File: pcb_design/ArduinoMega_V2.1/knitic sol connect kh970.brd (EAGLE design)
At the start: 40.9 x 35.5 mm, 18 parts

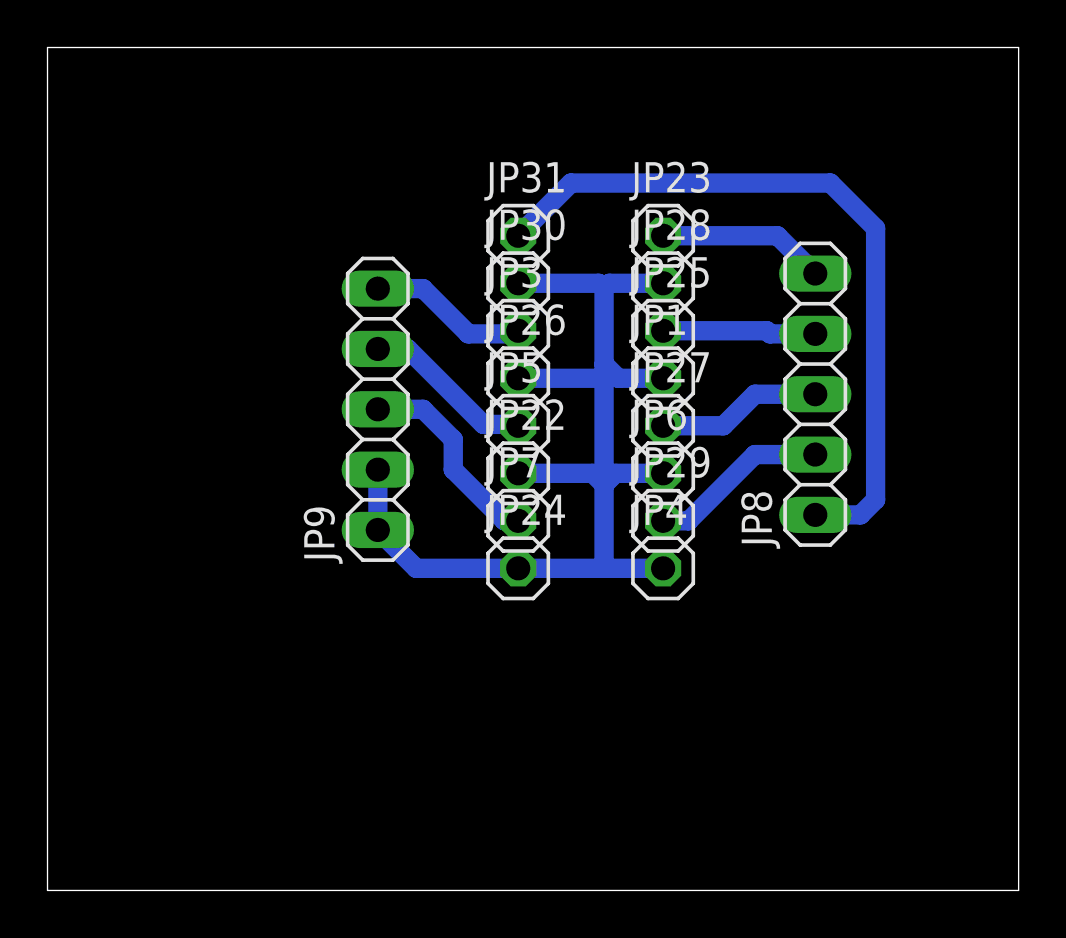
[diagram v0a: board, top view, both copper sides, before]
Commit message: Add info and reset/led on pcb design
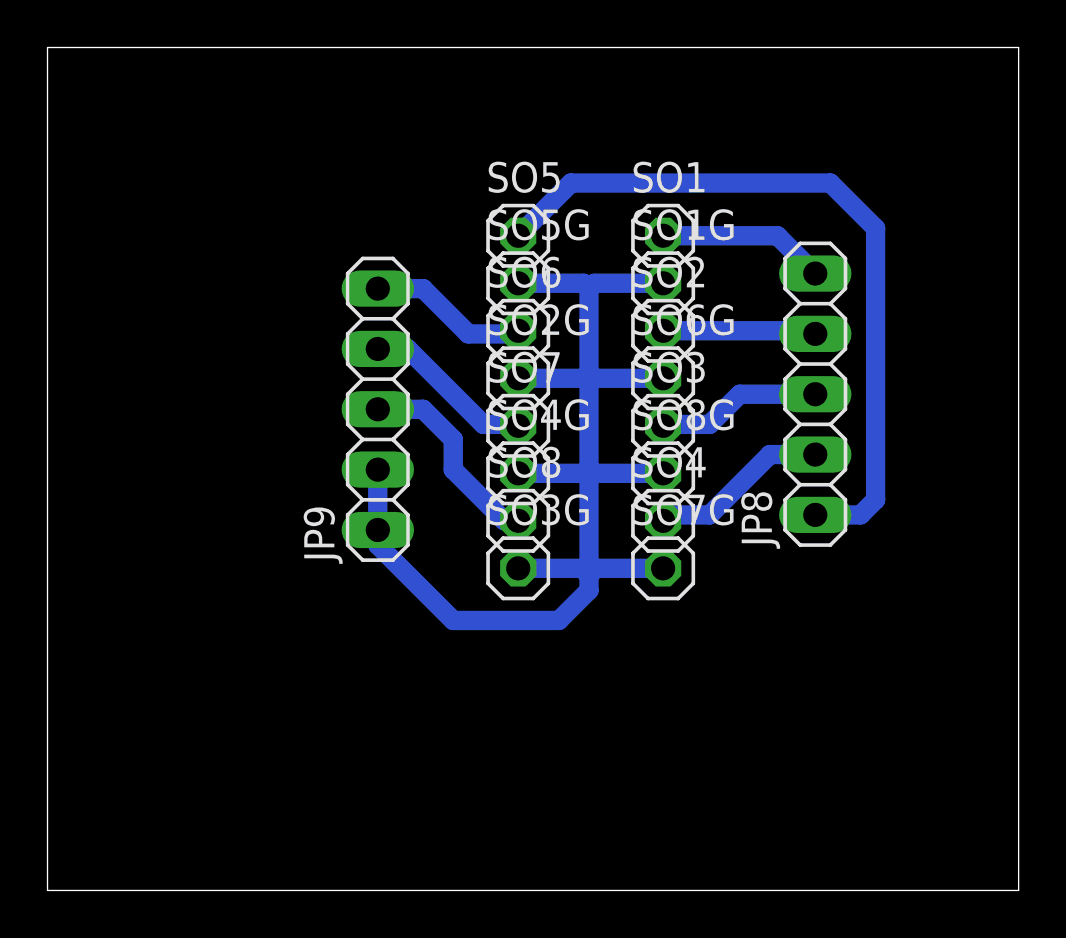
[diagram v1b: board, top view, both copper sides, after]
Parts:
- renumbered JP1 to SO6G, JP22 to SO4G, JP23 to SO1, JP24 to SO3G, JP25 to SO2, JP26 to SO2G, JP27 to SO3, JP28 to SO1G, JP29 to SO4, JP3 to SO6, JP30 to SO5G, JP31 to SO5, JP4 to SO7G, JP5 to SO7, JP6 to SO8G, JP7 to SO8
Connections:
- net N$4 renamed SO6G
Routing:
- net N$10: track 46.3 -> 51.6 mm
